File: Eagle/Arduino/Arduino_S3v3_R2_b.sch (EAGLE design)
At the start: 43 parts, among them IC1 ATMEGA8 (OR 168), J1 PORT D(D0-D7), J2 PORT C(A0-A5), J3 PORT B(D8-D13), Q1 16000, T1 BC547, T2 BC557

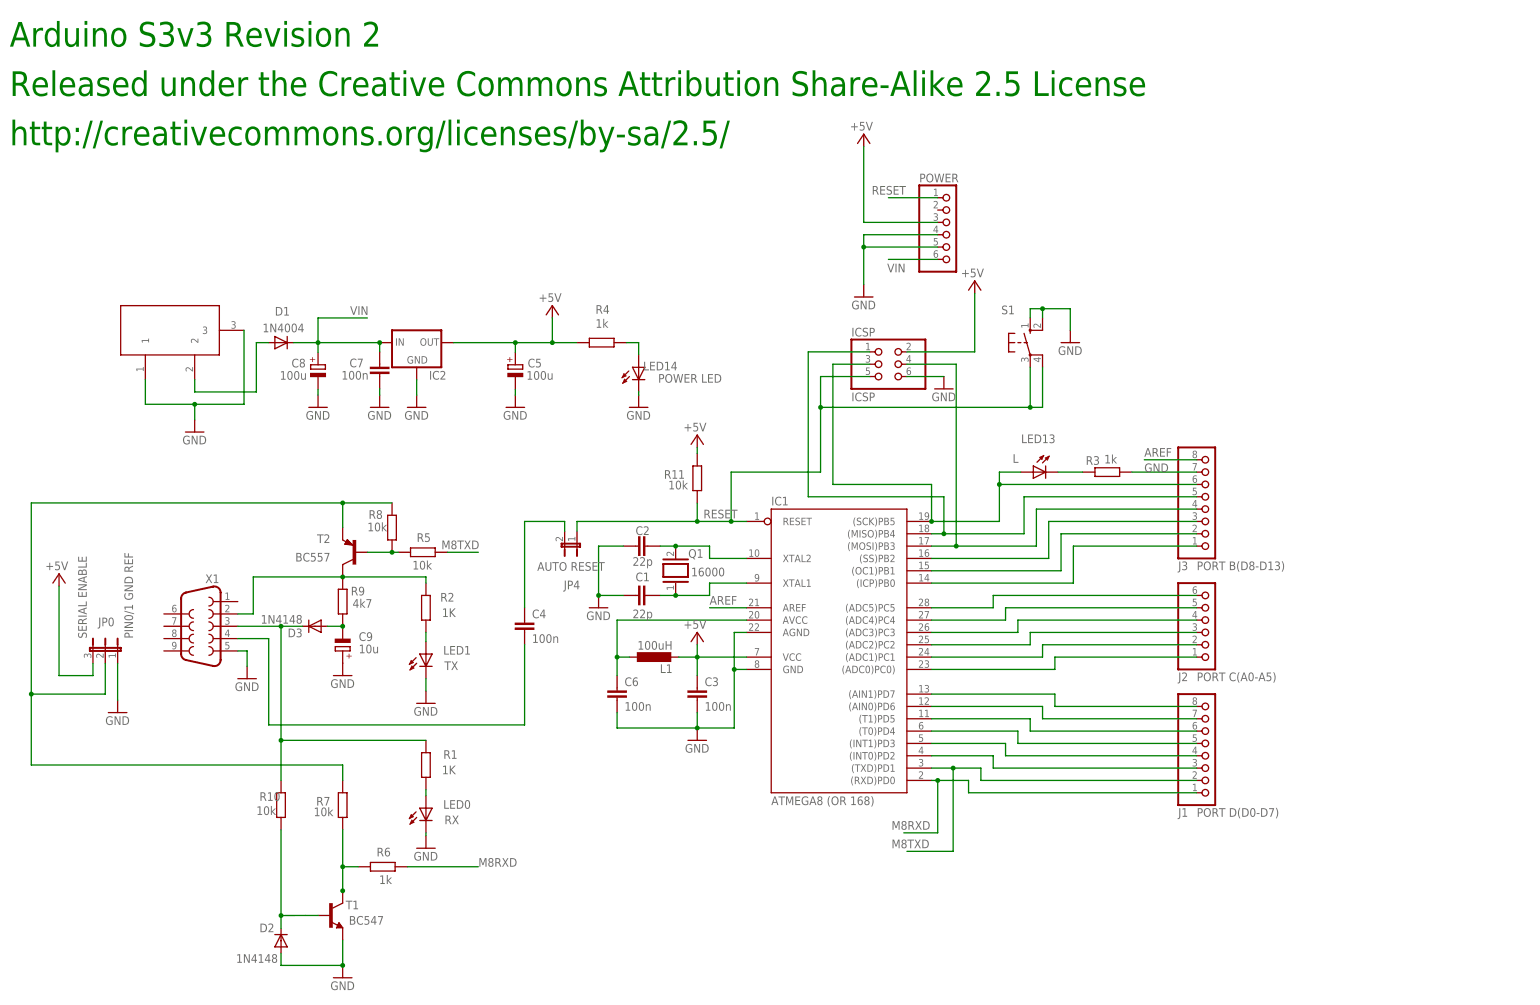
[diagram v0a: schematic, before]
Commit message: implemented gitview delete file - imroved eagle circiut for clock with measurement of current
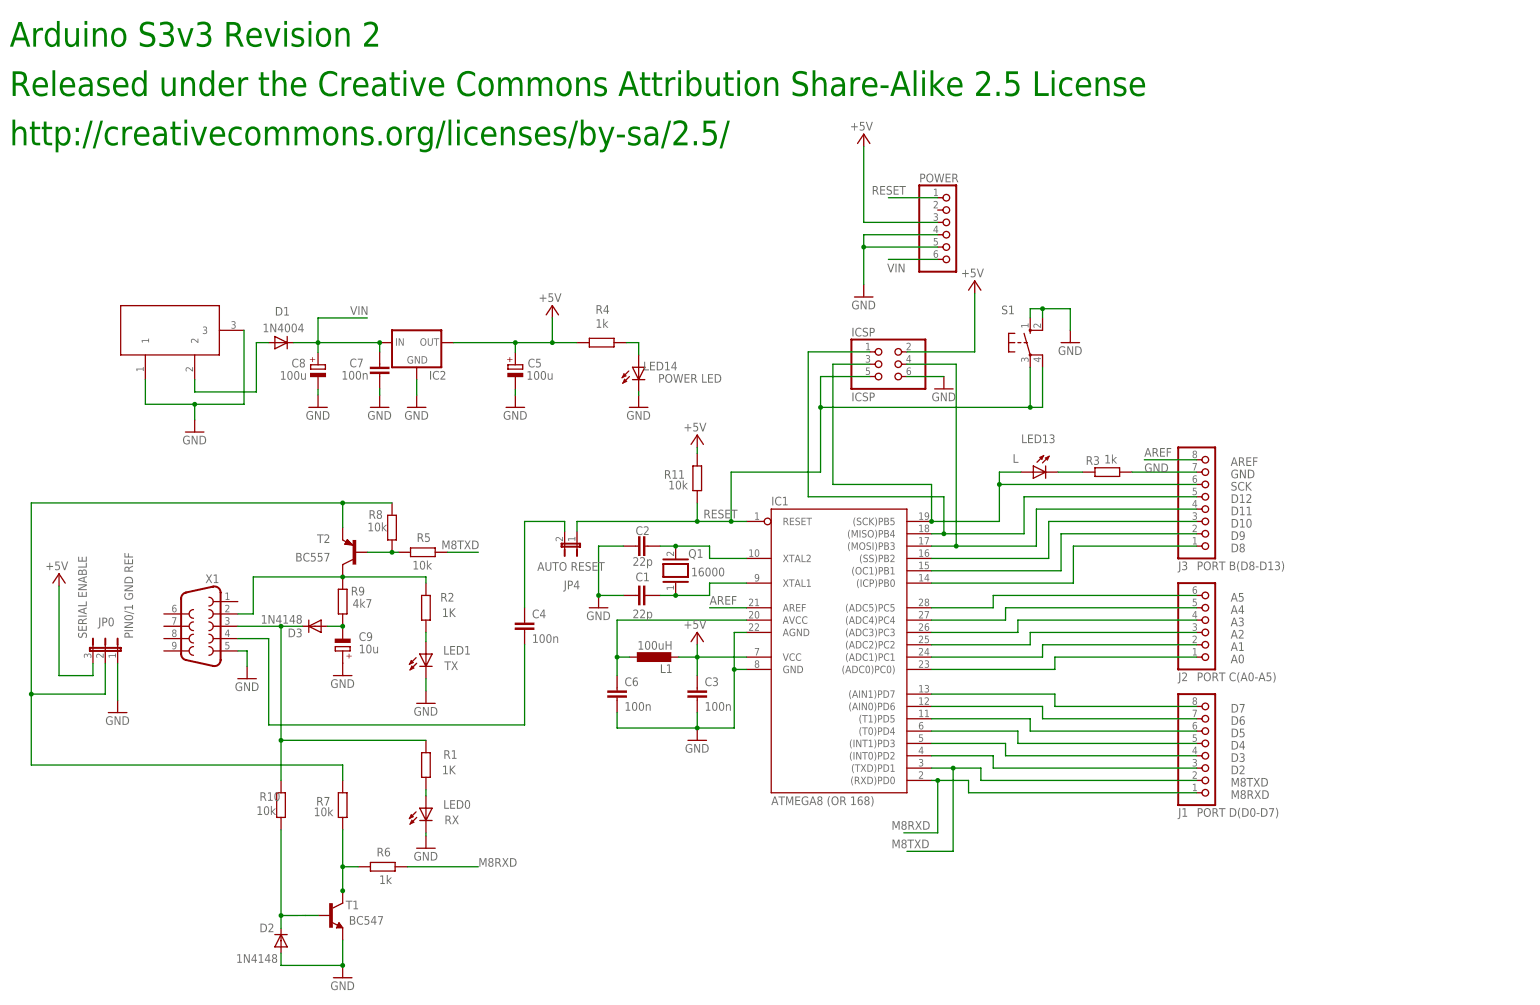
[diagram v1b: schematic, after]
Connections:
- net N$1 renamed D12
- net N$10 renamed D2
- net N$11 renamed D3
- net N$12 renamed D4
- net N$13 renamed D5
- net N$14 renamed D6
- net N$15 renamed D7
- net N$16 renamed A0
- net N$17 renamed A1
- net N$18 renamed A2
- net N$19 renamed A3
- net N$20 renamed A4
- net N$21 renamed A5
- net N$22 renamed D9
- net N$23 renamed D10
- net N$4 renamed D11
- net N$5 renamed D8

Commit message: Arduino-Eagle boards easyer basic design
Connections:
- net A4 renamed A4(SDA)
- net A5 renamed A5(SCL)
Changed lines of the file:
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@@
 </segment>
 </net>
-<net name="A4" class="0">
+<net name="A4(SDA)" class="0">
 <segment>
 <wire x1="257.175" y1="115.57" x2="217.805" y2="115.57" width="0.1524" layer="91"/>
@@
 </segment>
 </net>
-<net name="A5" class="0">
+<net name="A5(SCL)" class="0">
 <segment>
 <wire x1="202.565" y1="115.57" x2="215.265" y2="115.57" width="0.1524" layer="91"/>
